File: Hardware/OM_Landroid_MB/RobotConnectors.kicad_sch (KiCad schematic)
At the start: 27 parts, among them IC1 74ALVC164245DGG,11, J1 Conn_01x02_Pin, J11 Conn_01x03_Male, J12 Conn_01x03_Male, J13 Conn_01x03_Male, J14 Conn_01x03_Male, J17 Conn_01x02, J19 Conn_01x04, J2 Conn_02x04_Top_Bottom, J3 Conn_01x02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

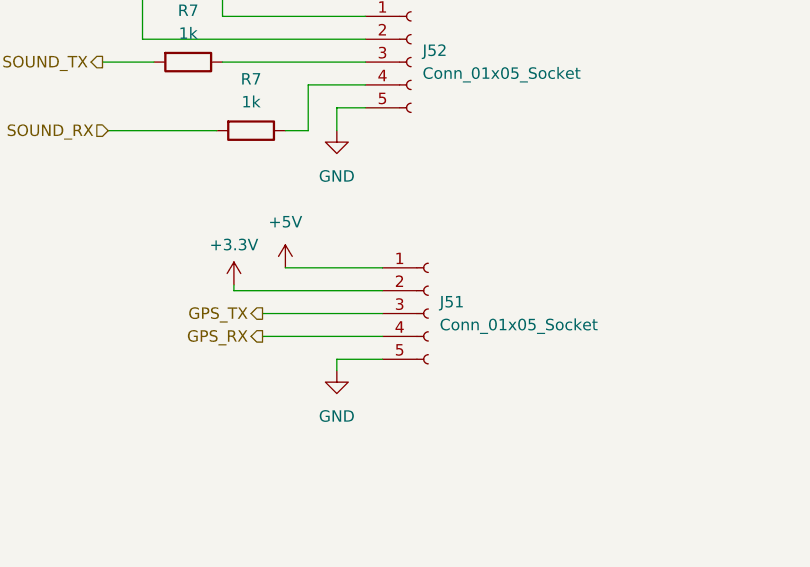
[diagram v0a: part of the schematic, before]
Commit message: Schematic update
Getting to grips with Github desktop...I worked out that I'd changed the PCB but had forgotten to update the schematic file for Kicad for the connectors  ....so there was a disconnect :)
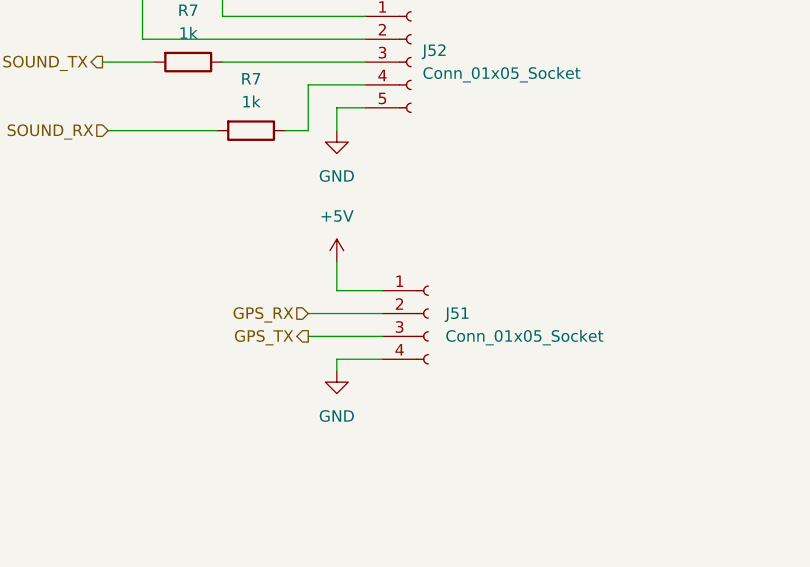
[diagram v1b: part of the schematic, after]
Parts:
- J51: symbol Connector:Conn_01x05_Socket -> Connector:Conn_01x04_Socket
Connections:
- net +3.3V is gone; now on net GPS_RX: J51.2 (Pin_2)
- net GND: now also J51.4 (Pin_4); no longer J51.5 (Pin_5)
- net GPS_RX: no longer J51.4 (Pin_4)

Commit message: Weekend progress
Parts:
- J51: footprint Connector_JST:JST_XH_B5B-XH-A_1x05_P2.50mm_Vertical -> Connector_JST:JST_XH_B4B-XH-AM_1x04_P2.50mm_Vertical
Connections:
- net GND: now also IC1.30 (2A4); no longer IC1.33 (2A2)
- net HALL_SWITCH_1: now also IC1.41 (1A4); no longer IC1.44 (1A2)
- net HALL_SWITCH_1_5V: now also IC1.8 (1B4), J13.2 (Pin_2); no longer IC1.5 (1B2), J11.2 (Pin_2)
- net HALL_SWITCH_2: now also IC1.40 (1A5); no longer IC1.43 (1A3)
- net HALL_SWITCH_2_5V: now also IC1.9 (1B5), J14.2 (Pin_2); no longer IC1.6 (1B3), J12.2 (Pin_2)
- net HALL_SWITCH_3: now also IC1.43 (1A3); no longer IC1.41 (1A4)
- net HALL_SWITCH_3_5V: now also IC1.6 (1B3), J12.2 (Pin_2); no longer IC1.8 (1B4), J13.2 (Pin_2)
- net HALL_SWITCH_4: now also IC1.44 (1A2); no longer IC1.40 (1A5)
- net HALL_SWITCH_4_5V: now also IC1.5 (1B2), J11.2 (Pin_2); no longer IC1.9 (1B5), J14.2 (Pin_2)
- net USS_1_ECHO: now also IC1.46 (1A1); no longer IC1.47 (1A0)
- net USS_1_ECHO_5V: now also IC1.3 (1B1); no longer IC1.2 (1B0)
- net USS_1_TRIGGER: now also IC1.33 (2A2); no longer IC1.30 (2A4)
- net USS_1_TRIGGER_5V: now also IC1.16 (2B2); no longer IC1.19 (2B4)
- net USS_2_ECHO: now also IC1.47 (1A0); no longer IC1.46 (1A1)
- net USS_2_ECHO_5V: now also IC1.2 (1B0); no longer IC1.3 (1B1)
- net at J52.3 (Pin_3): now also R7.1; no longer R7.1
- net at J52.4 (Pin_4): now also R7.1; no longer R7.1
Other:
- moved on the sheet: R7

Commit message: Finished Mainboard
Finished Mainboard redesign for OM Landroid
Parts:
- added J53: Conn_01x04_Socket, Connector_JST:JST_XH_B4B-XH-AM_1x04_P2.50mm_Vertical, symbol Connector:Conn_01x04_Socket
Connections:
- net +5V: now also J53.1 (Pin_1)
- net GND: now also J53.4 (Pin_4)
- new net Display SCL: J53.3 (Pin_3)
- new net Display SDA: J53.2 (Pin_2)
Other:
- moved on the sheet: J51
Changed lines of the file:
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@@
     (stroke (width 0) (type default))
   )
-  (wire (pts (xy 216.535 152.4) (xy 216.535 153.67))
+  (wire (pts (xy 175.514 152.908) (xy 175.514 154.178))
     (stroke (width 0) (type default))
   )
@@
     (stroke (width 0) (type default))
   )
+  (wire (pts (xy 246.888 152.146) (xy 234.95 152.146))
+    (stroke (width 0) (type default))
+  )
   (wire (pts (xy 29.21 34.29) (xy 26.035 34.29))
     (stroke (width 0) (type default))
@@
     (stroke (width 0) (type default))
   )
+  (wire (pts (xy 246.888 144.526) (xy 234.95 144.526))
+    (stroke (width 0) (type default))
+  )
   (wire (pts (xy 114.3 27.94) (xy 114.935 27.94))
     (stroke (width 0) (type default))
@@
     (stroke (width 0) (type default))
   )
-  (wire (pts (xy 221.615 144.78) (xy 216.535 144.78))
+  (wire (pts (xy 180.594 145.288) (xy 175.514 145.288))
     (stroke (width 0) (type default))
   )
@@
     (stroke (width 0) (type default))
   )
+  (wire (pts (xy 239.522 147.066) (xy 246.888 147.066))
+    (stroke (width 0) (type default))
+  )
   (wire (pts (xy 65.405 167.005) (xy 65.405 172.72))
     (stroke (width 0) (type default))
@@
     (stroke (width 0) (type default))
   )
+  (wire (pts (xy 234.95 144.526) (xy 234.95 139.7))
+    (stroke (width 0) (type default))
+  )
   (wire (pts (xy 55.88 108.585) (xy 55.88 116.205))
     (stroke (width 0) (type default))
@@
     (stroke (width 0) (type default))
   )
-  (wire (pts (xy 213.36 149.86) (xy 221.615 149.86))
+  (wire (pts (xy 172.339 150.368) (xy 180.594 150.368))
     (stroke (width 0) (type default))
   )
@@
     (stroke (width 0) (type default))
   )
+  (wire (pts (xy 246.888 149.606) (xy 239.268 149.606))
+    (stroke (width 0) (type default))
+  )
   (wire (pts (xy 242.57 39.37) (xy 236.22 39.37))
     (stroke (width 0) (type default))
@@
     (stroke (width 0) (type default))
   )
-  (wire (pts (xy 216.535 152.4) (xy 221.615 152.4))
+  (wire (pts (xy 175.514 152.908) (xy 180.594 152.908))
     (stroke (width 0) (type default))
   )
@@
     (stroke (width 0) (type default))
   )
-  (wire (pts (xy 216.535 141.605) (xy 216.535 144.78))
+  (wire (pts (xy 175.514 142.113) (xy 175.514 145.288))
     (stroke (width 0) (type default))
   )
@@
     (stroke (width 0) (type default))
   )
+  (wire (pts (xy 234.95 152.146) (xy 234.95 157.48))
+    (stroke (width 0) (type default))
+  )
   (wire (pts (xy 193.675 108.585) (xy 194.945 108.585))
     (stroke (width 0) (type default))
@@
     (stroke (width 0) (type default))
   )
-  (wire (pts (xy 213.36 147.32) (xy 221.615 147.32))
+  (wire (pts (xy 172.339 147.828) (xy 180.594 147.828))
     (stroke (width 0) (type default))
   )
@@
     (effects (font (size 1.27 1.27)) (justify right))
   )
-  (hierarchical_label "GPS_RX" (shape input) (at 213.36 147.32 180) (fields_autoplaced)
+  (hierarchical_label "GPS_RX" (shape input) (at 172.339 147.828 180) (fields_autoplaced)
     (effects (font (size 1.27 1.27)) (justify right))
   )
@@
     (effects (font (size 1.27 1.27)) (justify right))
   )
-  (hierarchical_label "GPS_TX" (shape output) (at 213.36 149.86 180) (fields_autoplaced)
+  (hierarchical_label "GPS_TX" (shape output) (at 172.339 150.368 180) (fields_autoplaced)
+    (effects (font (size 1.27 1.27)) (justify right))
+  )
+  (hierarchical_label "Display SCL" (shape output) (at 239.268 149.606 180) (fields_autoplaced)
     (effects (font (size 1.27 1.27)) (justify right))
   )
@@
   (hierarchical_label "MR_P1" (shape input) (at 63.5 52.07 0) (fields_autoplaced)
     (effects (font (size 1.27 1.27)) (justify left))
+  )
+  (hierarchical_label "Display SDA" (shape bidirectional) (at 239.522 147.066 180) (fields_autoplaced)
+    (effects (font (size 1.27 1.27)) (justify right))
   )
   (hierarchical_label "LED_TX" (shape output) (at 25.4 60.325 180) (fields_autoplaced)
@@
     )
   )
-  (symbol (lib_name "GND_2") (lib_id "power:GND") (at 216.535 153.67 0) (unit 1)
-    (in_bom yes) (on_board yes) (dnp no) (fields_autoplaced)
-    (property "Reference" "#PWR010" (at 216.535 160.02 0)
-      (effects (font (size 1.27 1.27)) hide)
-    )
-    (property "Value" "GND" (at 216.535 158.75 0)
-      (effects (font (size 1.27 1.27)))
-    )
-    (property "Footprint" "" (at 216.535 153.67 0)
-      (effects (font (size 1.27 1.27)) hide)
-    )
-    (property "Datasheet" "" (at 216.535 153.67 0)
+  (symbol (lib_name "GND_2") (lib_id "power:GND") (at 175.514 154.178 0) (unit 1)
+    (in_bom yes) (on_board yes) (dnp no) (fields_autoplaced)
+    (property "Reference" "#PWR010" (at 175.514 160.528 0)
+      (effects (font (size 1.27 1.27)) hide)
+    )
+    (property "Value" "GND" (at 175.514 159.258 0)
+      (effects (font (size 1.27 1.27)))
+    )
+    (property "Footprint" "" (at 175.514 154.178 0)
+      (effects (font (size 1.27 1.27)) hide)
+    )
+    (property "Datasheet" "" (at 175.514 154.178 0)
       (effects (font (size 1.27 1.27)) hide)
     )
@@
     )
   )
+  (symbol (lib_name "GND_3") (lib_id "power:GND") (at 234.95 157.48 0) (unit 1)
+    (in_bom yes) (on_board yes) (dnp no) (fields_autoplaced)
+    (property "Reference" "#PWR02" (at 234.95 163.83 0)
+      (effects (font (size 1.27 1.27)) hide)
+    )
+    (property "Value" "GND" (at 234.95 162.56 0)
+      (effects (font (size 1.27 1.27)))
+    )
+    (property "Footprint" "" (at 234.95 157.48 0)
+      (effects (font (size 1.27 1.27)) hide)
+    )
+    (property "Datasheet" "" (at 234.95 157.48 0)
+      (effects (font (size 1.27 1.27)) hide)
+    )
+    (pin "1")
+    (instances
+      (project "OM Landroid MB"
+        (path "/c454102f-dc92-4550-9492-797fc8e6b49c/00000000-0000-0000-0000-000061040c60"
+          (reference "#PWR02") (unit 1)
+        )
+      )
+    )
+  )
   (symbol (lib_id "power:GND") (at 55.88 179.705 0) (unit 1)
     (in_bom yes) (on_board yes) (dnp no) (fields_autoplaced)
@@
         (path "/c454102f-dc92-4550-9492-797fc8e6b49c/00000000-0000-0000-0000-000061040c60"
           (reference "#PWR0153") (unit 1)
+        )
+      )
+    )
+  )
+  (symbol (lib_name "+5V_2") (lib_id "power:+5V") (at 234.95 139.7 0) (unit 1)
+    (in_bom yes) (on_board yes) (dnp no) (fields_autoplaced)
+    (property "Reference" "#PWR01" (at 234.95 143.51 0)
+      (effects (font (size 1.27 1.27)) hide)
+    )
+    (property "Value" "+5V" (at 234.95 134.62 0)
+      (effects (font (size 1.27 1.27)))
+    )
+    (property "Footprint" "" (at 234.95 139.7 0)
+      (effects (font (size 1.27 1.27)) hide)
+    )
+    (property "Datasheet" "" (at 234.95 139.7 0)
+      (effects (font (size 1.27 1.27)) hide)
+    )
+    (pin "1")
+    (instances
+      (project "OM Landroid MB"
+        (path "/c454102f-dc92-4550-9492-797fc8e6b49c/00000000-0000-0000-0000-000061040c60"
+          (reference "#PWR01") (unit 1)
         )
       )
@@
     )
   )
-  (symbol (lib_id "Connector:Conn_01x04_Socket") (at 226.695 147.32 0) (unit 1)
-    (in_bom yes) (on_board yes) (dnp no) (fields_autoplaced)
-    (property "Reference" "J51" (at 228.6 147.32 0)
+  (symbol (lib_id "Connector:Conn_01x04_Socket") (at 185.674 147.828 0) (unit 1)
+    (in_bom yes) (on_board yes) (dnp no) (fields_autoplaced)
+    (property "Reference" "J51" (at 187.579 147.828 0)
       (effects (font (size 1.27 1.27)) (justify left))
     )
-    (property "Value" "Conn_01x05_Socket" (at 228.6 149.86 0)
+    (property "Value" "Conn_01x05_Socket" (at 187.579 150.368 0)
       (effects (font (size 1.27 1.27)) (justify left))
     )
-    (property "Footprint" "Connector_JST:JST_XH_B4B-XH-AM_1x04_P2.50mm_Vertical" (at 226.695 147.32 0)
-      (effects (font (size 1.27 1.27)) hide)
-    )
-    (property "Datasheet" "~" (at 226.695 147.32 0)
+    (property "Footprint" "Connector_JST:JST_XH_B4B-XH-AM_1x04_P2.50mm_Vertical" (at 185.674 147.828 0)
+      (effects (font (size 1.27 1.27)) hide)
+    )
+    (property "Datasheet" "~" (at 185.674 147.828 0)
       (effects (font (size 1.27 1.27)) hide)
     )
@@
     )
   )
-  (symbol (lib_name "+5V_1") (lib_id "power:+5V") (at 216.535 141.605 0) (unit 1)
-    (in_bom yes) (on_board yes) (dnp no) (fields_autoplaced)
-    (property "Reference" "#PWR011" (at 216.535 145.415 0)
-      (effects (font (size 1.27 1.27)) hide)
-    )
-    (property "Value" "+5V" (at 216.535 136.525 0)
-      (effects (font (size 1.27 1.27)))
-    )
-    (property "Footprint" "" (at 216.535 141.605 0)
-      (effects (font (size 1.27 1.27)) hide)
-    )
-    (property "Datasheet" "" (at 216.535 141.605 0)
+  (symbol (lib_name "+5V_1") (lib_id "power:+5V") (at 175.514 142.113 0) (unit 1)
+    (in_bom yes) (on_board yes) (dnp no) (fields_autoplaced)
+    (property "Reference" "#PWR011" (at 175.514 145.923 0)
+      (effects (font (size 1.27 1.27)) hide)
+    )
+    (property "Value" "+5V" (at 175.514 137.033 0)
+      (effects (font (size 1.27 1.27)))
+    )
+    (property "Footprint" "" (at 175.514 142.113 0)
+      (effects (font (size 1.27 1.27)) hide)
+    )
+    (property "Datasheet" "" (at 175.514 142.113 0)
       (effects (font (size 1.27 1.27)) hide)
     )
@@
         )
       )
+    )
+  )
+  (symbol (lib_id "Connector:Conn_01x04_Socket") (at 251.968 147.066 0) (unit 1)
+    (in_bom yes) (on_board yes) (dnp no) (fields_autoplaced)
+    (property "Reference" "J53" (at 252.73 147.066 0)
+      (effects (font (size 1.27 1.27)) (justify left))
+    )
+    (property "Value" "Conn_01x04_Socket" (at 252.73 149.606 0)
+      (effects (font (size 1.27 1.27)) (justify left))
+    )
+    (property "Footprint" "Connector_JST:JST_XH_B4B-XH-AM_1x04_P2.50mm_Vertical" (at 251.968 147.066 0)
+      (effects (font (size 1.27 1.27)) hide)
+    )
+    (property "Datasheet" "~" (at 251.968 147.066 0)
+      (effects (font (size 1.27 1.27)) hide)
+    )
+    (pin "1")
+    (pin "2")
+    (pin "3")
+    (pin "4")
+    (instances
+      (project "OM Landroid MB"
+        (path "/c454102f-dc92-4550-9492-797fc8e6b49c/00000000-0000-0000-0000-000061040c60"
+          (reference "J53") (unit 1)
+        )
+      )

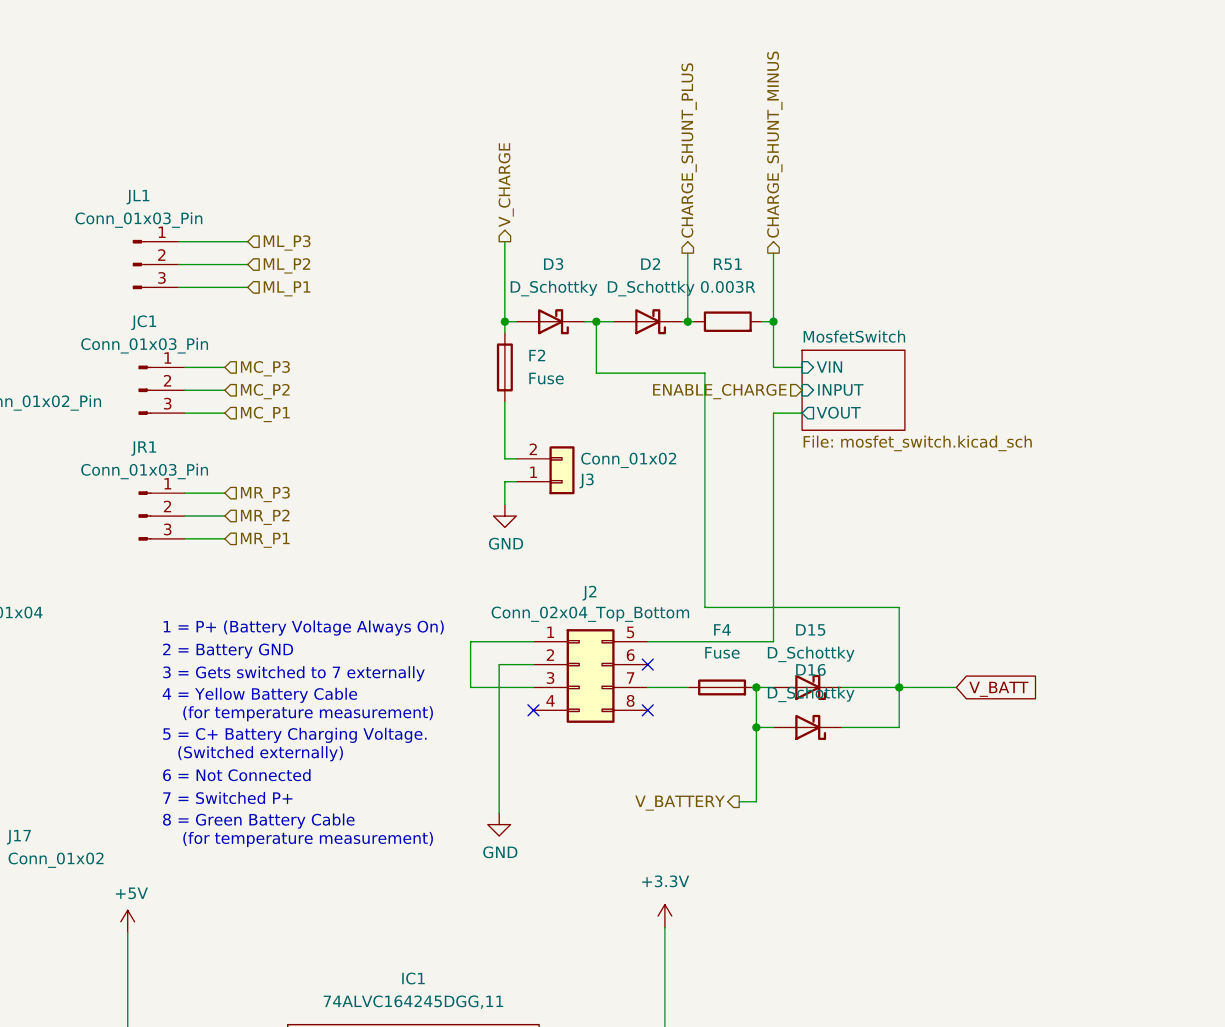
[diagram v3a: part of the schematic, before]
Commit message: Updates and revisions to charging connections
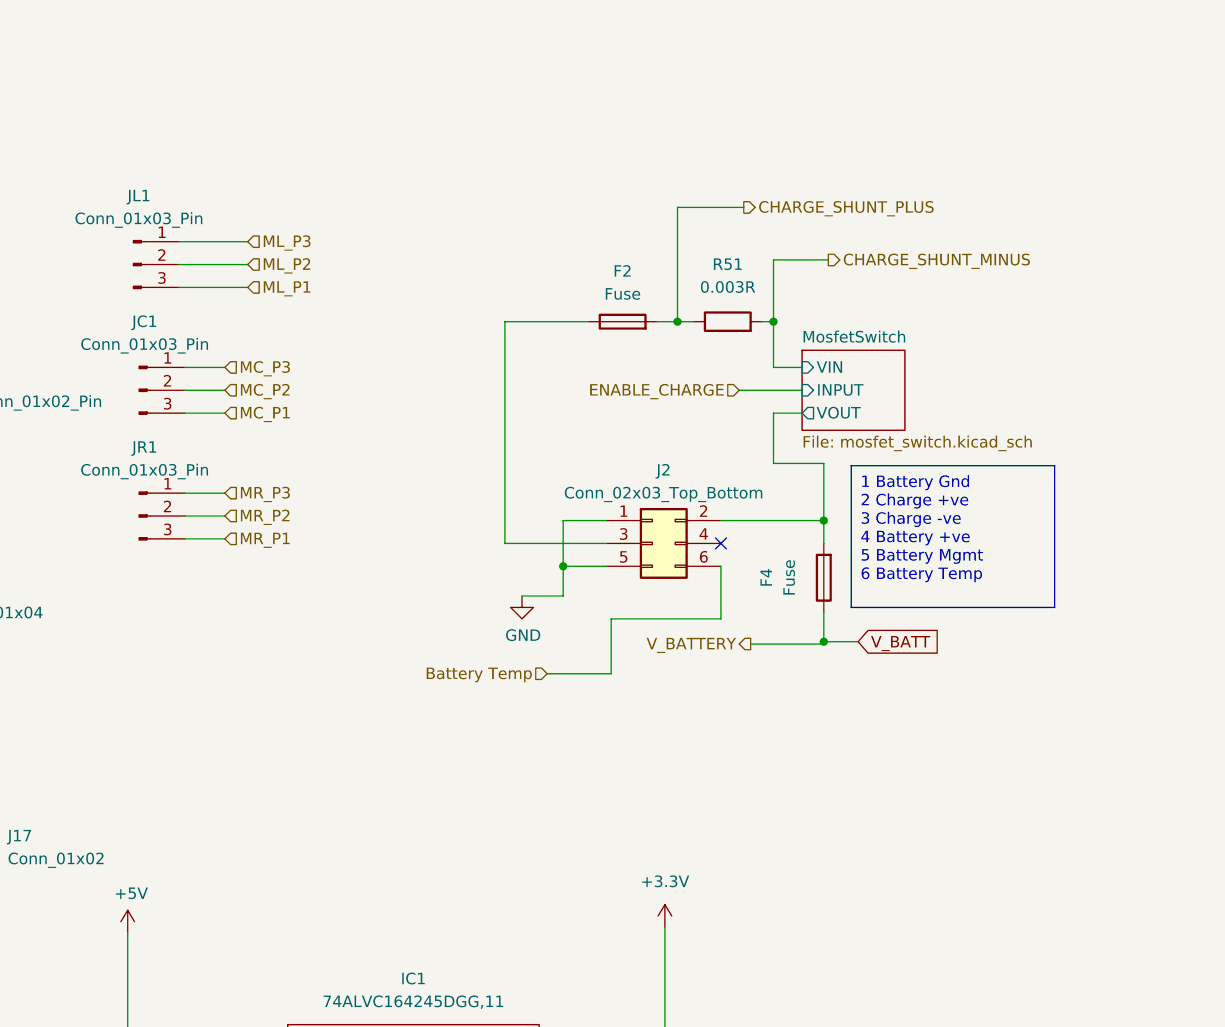
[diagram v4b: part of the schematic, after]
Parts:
- removed D15, D16, D2, D3: D_Schottky, Diode_SMD:D_SMA_Handsoldering, symbol Device:D_Schottky
- removed J2: Conn_02x04_Top_Bottom, Connector_Molex:Molex_Mini-Fit_Jr_5566-08A_2x04_P4.20mm_Vertical, symbol Connector_Generic:Conn_02x04_Top_Bottom
- removed J3: Conn_01x02, Connector_Molex:Molex_Mini-Fit_Jr_5566-02A_2x01_P4.20mm_Vertical, symbol Connector_Generic:Conn_01x02
- added J2: Conn_02x03_Top_Bottom, Landroid_Motor_Conn:TE_179841, symbol Connector_Generic:Conn_02x03_Odd_Even
- JC1, JL1, JR1: footprint Connector_Molex:Molex_KK-254_AE-6410-03A_1x03_P2.54mm_Vertical -> Landroid_Motor_Conn:TE_179839
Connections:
- net V_BATTERY is gone; now on net MosfetSwitch/VOUT: F4.2
- net CHARGE_SHUNT_PLUS: now also F2.2
- net GND: now also J2.1 (Pin_1), J2.5 (Pin_5)
- net MosfetSwitch/VOUT: now also J2.2 (Pin_2)
- net V_BATT: now also F4.1
- net V_CHARGE: no longer names the net of F2.1
- net V_CHARGE: now also J2.3 (Pin_3)
- new net Battery Temp: J2.6 (Pin_6)
- no-connect marks 11 -> 9
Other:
- note removed: "1 = P+ (Battery Voltage Always On)"
- note removed: "2 = Battery GND"
- note removed: "3 = Gets switched to 7 externally"
- note removed: "4 = Yellow Battery Cable (for temperature measurement)"
- note removed: "5 = C+ Battery Charging Voltage. (Switched externally)"
- note removed: "6 = Not Connected"
- note removed: "7 = Switched P+"
- note removed: "8 = Green Battery Cable (for temperature measurement)"
- moved on the sheet: F2, F4

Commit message: Changes to align BOM with board
Changes were needed to  align the BOM content with the board and to reflect component availability from Digikey
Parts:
- JC1, JL1, JR1: Digikey (none) -> A107226-ND
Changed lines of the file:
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@@
+      (effects (font (size 1.27 1.27)) hide)
+    )
+    (property "Digikey" "A107226-ND" (at 53.975 35.56 0)
       (effects (font (size 1.27 1.27)) hide)
     )
@@
       (effects (font (size 1.27 1.27)) hide)
     )
+    (property "Digikey" "A107226-ND" (at 53.975 49.53 0)
+      (effects (font (size 1.27 1.27)) hide)
+    )
     (pin "1")
     (pin "2")
@@
       (effects (font (size 1.27 1.27)) hide)
     )
+    (property "Digikey" "A107226-ND" (at 53.34 21.59 0)
+      (effects (font (size 1.27 1.27)) hide)
+    )
